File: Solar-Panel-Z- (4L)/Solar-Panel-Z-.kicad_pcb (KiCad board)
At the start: 4 copper layers, 48.4 x 48.4 mm, 88 parts, among them J1 FTS-105-01-L-DV-A, J2 U.FL-R-SMT-1, Q1 BSS138DWQ-7, Q2 MBT2222ADW1T1, Q3 BSS138DWQ-7, Q4 MBT2222ADW1T1, Q5 IRLML2803, U1 BQ25570RGRR, U2 TSL2561, U3 ATB2012-50011-T000, U4 NDS8434

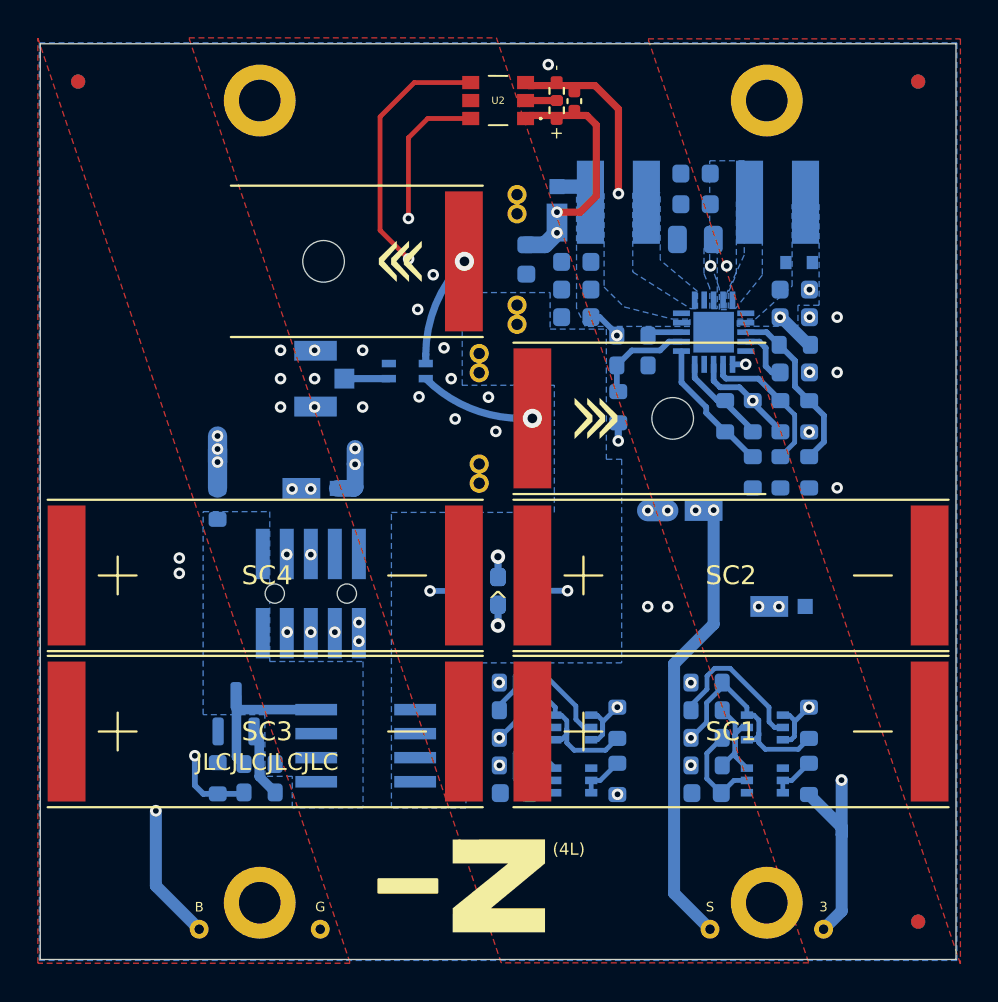
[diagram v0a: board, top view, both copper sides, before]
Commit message: Changed design to TSL2691 and IRF7404 on Z- (4L)
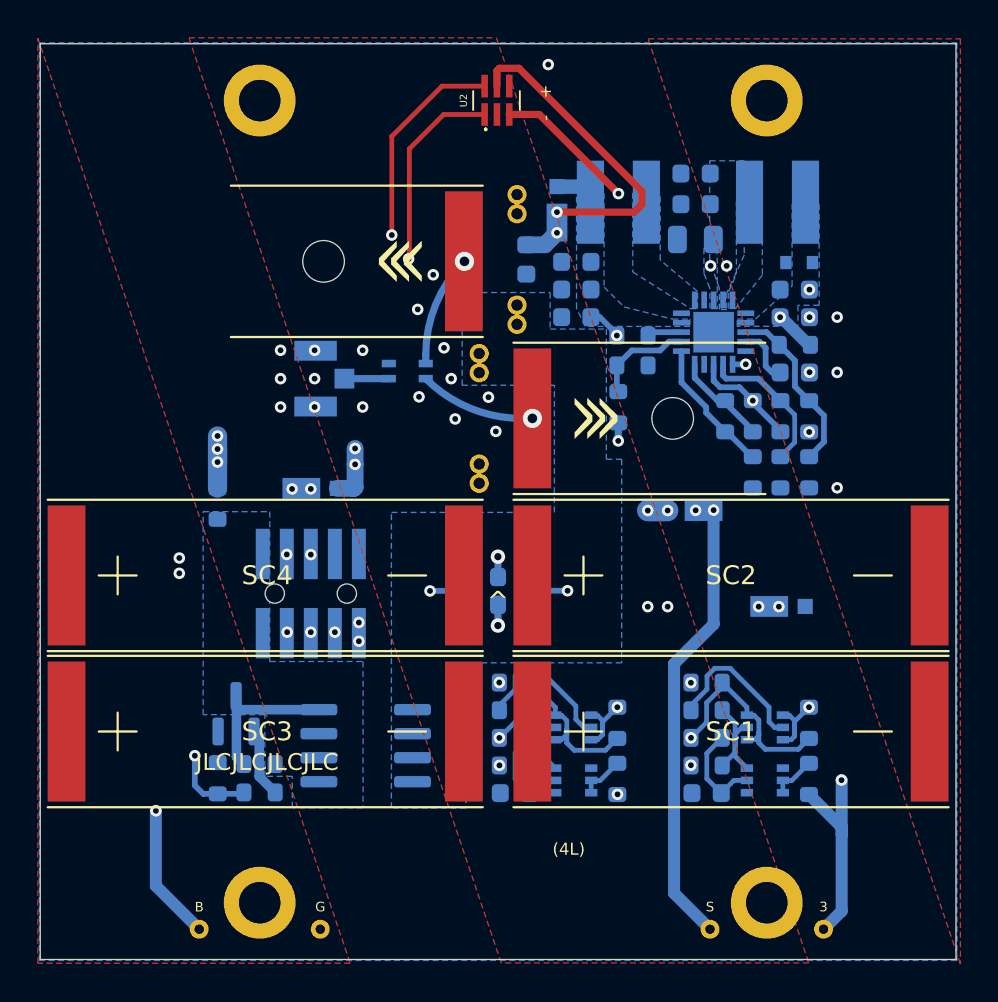
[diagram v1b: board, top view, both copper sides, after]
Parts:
- removed C1: 1uF, Capacitor_SMD:C_0402_1005Metric
- removed R1, R2: 0, Resistor_SMD:R_0402_1005Metric
- removed REF** (x6): Fiducial_0.75mm_Mask1.5mm, Fiducial:Fiducial_0.75mm_Mask1.5mm
- removed Ref**: Val**, custom-footprints:ypanel
- removed Ref**: Val**, custom-footprints:pycubed_mini_half
- U2: value TSL2561 -> TSL2591; footprint solarpanels:TSL2561 -> solarpanels:TSL2591
- U4: value NDS8434 -> IRF7404; footprint solarpanels:NDS8434 -> Package_SO:SOIC-8_3.9x4.9mm_P1.27mm
- turned U2 to 90 degrees
- turned U4 to 0 degrees
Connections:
- R5 pad 1: Net-(R5-Pad1) -> Net-(R10-Pad2)
- R6 pad 2: Net-(R5-Pad1) -> Net-(R10-Pad2)
- U1 pad 7: Net-(R5-Pad1) -> Net-(R10-Pad2)
- U2 pad 1: +3V3 -> SCL_LS
- U2 pad 2: Net-(R1-Pad1) -> unconnected-(U2-Pad2)
- U2 pad 4: SCL_LS -> unconnected-(U2-Pad4)
- U2 pad 5: unconnected-(U2-Pad5) -> +3V3
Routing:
- net Net-(R10-Pad2): track 17.1 -> 24.9 mm
- net Net-(R5-Pad1): track 7.76 -> 0.00 mm
- net +3V3: track 23.0 -> 29.6 mm
- net SCL_LS: track 62.3 -> 59.2 mm
- net GND: track 9.73 -> 7.51 mm
- net SDA_LS: track 49.8 -> 51.8 mm
- net Net-(R1-Pad1): track 1.64 -> 0.00 mm

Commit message: Changed TSL2591 to BH1750
All boards (4L) except -Y
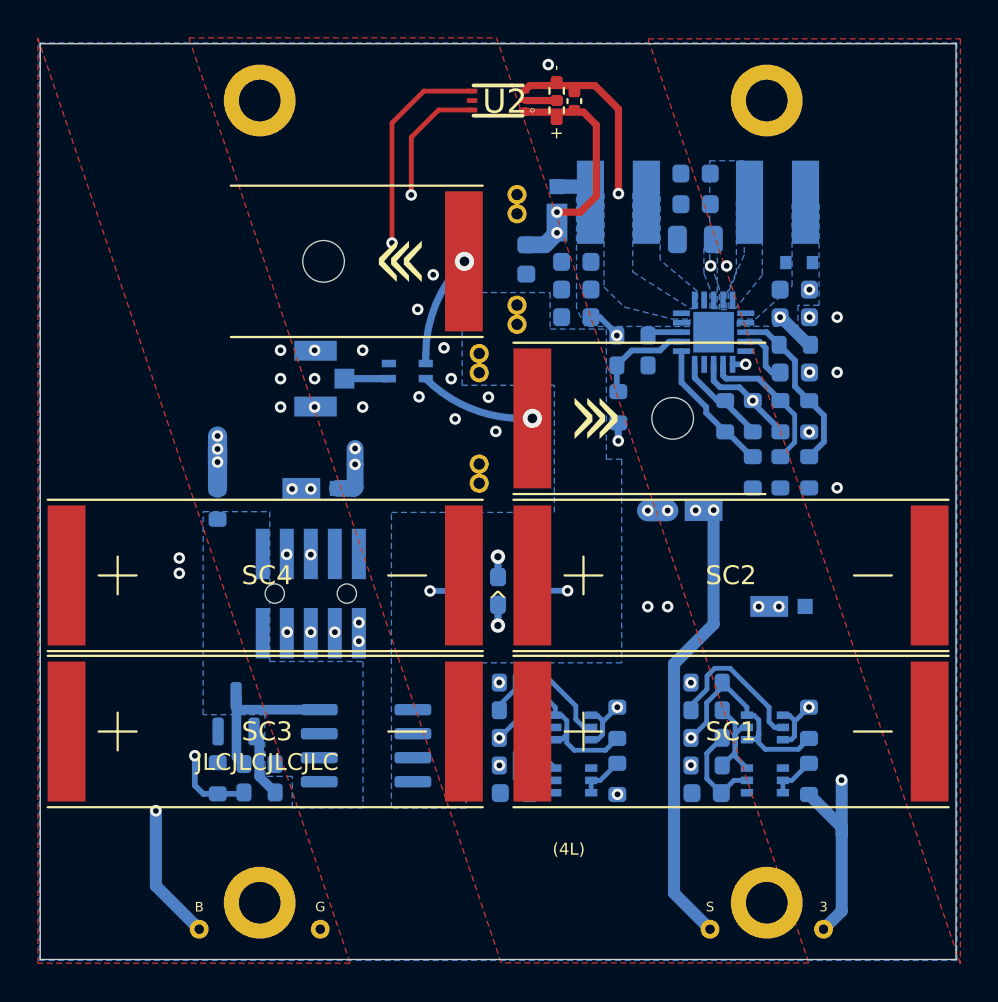
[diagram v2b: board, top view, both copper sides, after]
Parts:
- added C1: 1uF, Capacitor_SMD:C_0402_1005Metric, F.Cu at (110.7, 45.3)
- added R1: 0, Resistor_SMD:R_0402_1005Metric, F.Cu at (109.8, 45.8)
- added R2: 0, Resistor_SMD:R_0402_1005Metric, F.Cu at (109.8, 44.8)
- U2: value TSL2591 -> BH1750FVI-TR; footprint solarpanels:TSL2591 -> solarpanels:WSOF6
- turned U2 to 180 degrees
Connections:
- U2 pad 1: SCL_LS -> +3V3
- U2 pad 2: unconnected-(U2-Pad2) -> Net-(R1-Pad1)
- U2 pad 4: unconnected-(U2-Pad4) -> SDA_LS
- U2 pad 5: +3V3 -> unconnected-(U2-Pad5)
- U2 pad 6: SDA_LS -> SCL_LS
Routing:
- net +3V3: track 29.6 -> 23.3 mm
- net GND: track 7.51 -> 10.0 mm
- net Net-(R1-Pad1): track 0.00 -> 1.64 mm

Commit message: Updated light sensor to OPT 3001, Updated solar diodes.
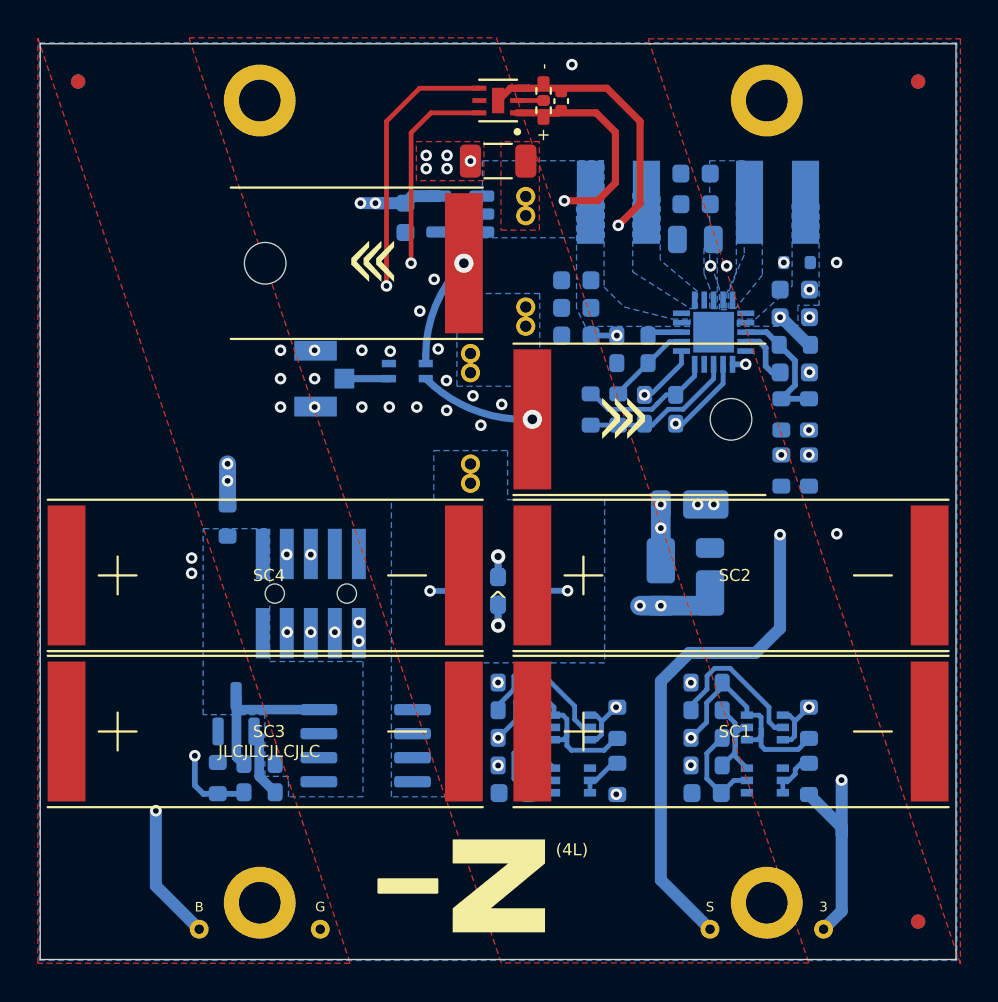
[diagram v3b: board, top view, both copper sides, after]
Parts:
- removed D5: MSS1P4-M3_89A, solarpanels:MICROSMP
- removed R31: 10K, Resistor_SMD:R_0603_1608Metric
- added Q6: IRF7404, Package_SO:SOIC-8_3.9x4.9mm_P1.27mm, B.Cu at (99.7, 79.4)
- added R34: 100K, Resistor_SMD:R_0603_1608Metric, B.Cu at (94.1, 80.4)
- added R35: 1R, Resistor_SMD:R_1206_3216Metric, F.Cu at (106.7, 48.5)
- added REF**: Fiducial_0.75mm_Mask1.5mm, Fiducial:Fiducial_0.75mm_Mask1.5mm, F.Cu at (128.9, 88.7)
- added REF**: Fiducial_0.75mm_Mask1.5mm, Fiducial:Fiducial_0.75mm_Mask1.5mm, F.Cu at (128.9, 44.3)
- added REF**: Fiducial_0.75mm_Mask1.5mm, Fiducial:Fiducial_0.75mm_Mask1.5mm, F.Cu at (84.5, 44.3)
- added REF**: Fiducial_0.75mm_Mask1.5mm, Fiducial:Fiducial_0.75mm_Mask1.5mm, B.Cu at (128.9, 44.3)
- added REF**: Fiducial_0.75mm_Mask1.5mm, Fiducial:Fiducial_0.75mm_Mask1.5mm, B.Cu at (128.9, 88.7)
- added REF**: Fiducial_0.75mm_Mask1.5mm, Fiducial:Fiducial_0.75mm_Mask1.5mm, B.Cu at (84.5, 44.3)
- added Ref**: Val**, custom-footprints:ypanel, F.Cu at (106.1, 86.6)
- added Ref**: Val**, custom-footprints:pycubed_mini_half, B.Cu at (106.8, 44.6)
- D2, D3, D4: value MSS1P4-M3_89A -> DFLS130L-7; footprint solarpanels:MICROSMP -> Diode_SMD:D_PowerDI-123
- J1: value FTS-105-01-L-DV-A -> FTS-105-01-X-DV-A
- J2: footprint solarpanels:U.FL-R-SMT-1 -> mainboard:U.FL-R-SMT-1
- JP1: value Jumper -> BurnWire 1
- JP2: value Jumper -> BurnWire 2
- Q1, Q3: value BSS138DWQ-7 -> NX3008NBKS
- R1, R12, R13, R16, R17, R18, R2, R3, R4: value 0 -> 0R
- R14, R15, R19, R20: value DNI -> DNI (0R)
- R21, R26: value 680 -> 680R
- R32: value 4.7K -> 10K
- R33: value 100K -> 4.7K
- U2: value BH1750FVI-TR -> OPT3001; footprint solarpanels:WSOF6 -> solarpanels:OPT3001
- U4: value IRF7404 -> MAX40200AUK; footprint Package_SO:SOIC-8_3.9x4.9mm_P1.27mm -> Package_TO_SOT_SMD:SOT-23-5
- moved U4 28.5 mm to (104.7, 51.3), turned to 180 degrees
- moved D4 18.9 mm to (115.3, 70.5), turned to -90 degrees
- moved D2 17.1 mm to (116.8, 66.7), turned to 180 degrees
- moved JP1 8.75 mm to (105.2, 62.1)
- moved JP2 8.66 mm to (108.2, 53.8), turned to 0 degrees
- moved R7 8.58 mm to (111.6, 61.6), turned to -90 degrees
- moved C11 6.76 mm to (101.8, 51.5)
- moved R5 6.37 mm to (115.3, 62.4), turned to 180 degrees
- moved D3 4.09 mm to (117.9, 70.5), turned to 90 degrees
- moved R8 3.62 mm to (115.3, 60.9), turned to 0 degrees
- moved R15 3.39 mm to (121.7, 61.9)
- moved R32 2.34 mm to (91.9, 81.1), turned to 90 degrees
- moved R9 1.51 mm to (121.7, 64.9)
- moved R6 1.51 mm to (123.1, 64.9)
- moved R33 1.49 mm to (94.1, 81.9), turned to 180 degrees
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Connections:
- C10 pad 1: Net-(C10-Pad1) -> Net-(U1-VOUT)
- C8 pad 1: Net-(C10-Pad1) -> Net-(U1-VOUT)
- D2 pad 1: +3V3 -> VSOLAR
- D2 pad 2: Net-(C10-Pad1) -> /VSOLAR_FULL
- JP1 pad 2: GND -> Net-(JP1-Pad2)
- JP2 pad 1: /VBURN -> Net-(JP1-Pad2)
- JP2 pad 2: GND -> Net-(JP2-Pad2)
- L2 pad 2: Net-(C10-Pad1) -> Net-(U1-VOUT)
- Q5 pad 1: Net-(Q5-Pad1) -> Net-(Q5-G)
- Q5 pad 3: Net-(Q5-Pad3) -> Net-(Q5-D)
- R10 pad 2: Net-(R10-Pad2) -> Net-(U1-VRDIV)
- R32 pad 1: Net-(Q5-Pad1) -> BURN1
- R32 pad 2: BURN1 -> GND
- R33 pad 1: Net-(Q5-Pad3) -> Net-(Q5-G)
- R33 pad 2: BATT_P -> BURN1
- R5 pad 1: Net-(R10-Pad2) -> Net-(U1-VBAT_OV)
- R5 pad 2: Net-(R10-Pad2) -> Net-(U1-VRDIV)
- R6 pad 2: Net-(R10-Pad2) -> Net-(U1-VBAT_OV)
- R7 pad 2: Net-(R10-Pad2) -> Net-(U1-VRDIV)
- U1 pad 14: Net-(C10-Pad1) -> Net-(U1-VOUT)
- U1 pad 7: Net-(R10-Pad2) -> Net-(U1-VBAT_OV)
- U1 pad 8: Net-(R10-Pad2) -> Net-(U1-VRDIV)
- U2 pad 4: SDA_LS -> SCL_LS
- U2 pad 6: SCL_LS -> SDA_LS
- U4 pad 1: BATT_P -> Net-(U1-VOUT)
- U4 pad 2: BATT_P -> GND
- U4 pad 3: BATT_P -> Net-(U1-VOUT)
- U4 pad 4: Net-(Q5-Pad3) -> unconnected-(U4-NC-Pad4)
- U4 pad 5: /VBURN -> +3V3
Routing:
- net Net-(R10-Pad2): track 24.9 -> 0.00 mm, vias 2 -> 0
- net Net-(U1-VBAT_OV): track 0.00 -> 15.7 mm, vias 0 -> 2
- net VSOLAR: track 43.6 -> 56.7 mm, vias 4 -> 5
- net Net-(Q5-Pad3): track 8.70 -> 0.00 mm
- net Net-(Q5-D): track 0.00 -> 8.70 mm
- net Net-(U1-VRDIV): track 0.00 -> 8.28 mm
- net SCL_LS: track 59.0 -> 65.5 mm
- net Net-(U1-OK_PROG): track 7.08 -> 13.0 mm, vias 0 -> 2
- net Net-(D3-K): track 9.94 -> 4.38 mm, vias 6 -> 2
- net GND: track 10.0 -> 15.1 mm, vias 22 -> 30
- net +3V3: track 23.3 -> 28.3 mm, vias 10 -> 11
- net SDA_LS: track 51.4 -> 55.2 mm
- net Net-(Q5-Pad1): track 3.68 -> 0.00 mm
- net Net-(Q5-G): track 0.00 -> 3.68 mm
- net Net-(U1-OK_HYST): track 4.89 -> 7.23 mm
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- added copper zone on In1.Cu, net GND
- added copper zone on B.Cu, net Net-(JP1-Pad2)
- added copper zone on In1.Cu, net Net-(JP1-Pad2)
- added copper zone on F.Cu, net Net-(JP2-Pad2)
- added copper zone on B.Cu, net Net-(U1-VOUT)
- removed copper zone on B.Cu, net Net-(C10-Pad1)
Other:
- board text added: "Rev B3/01"
- board text removed: "Rev B2/01"

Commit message: Silkscreen fix for -Z antenna wire
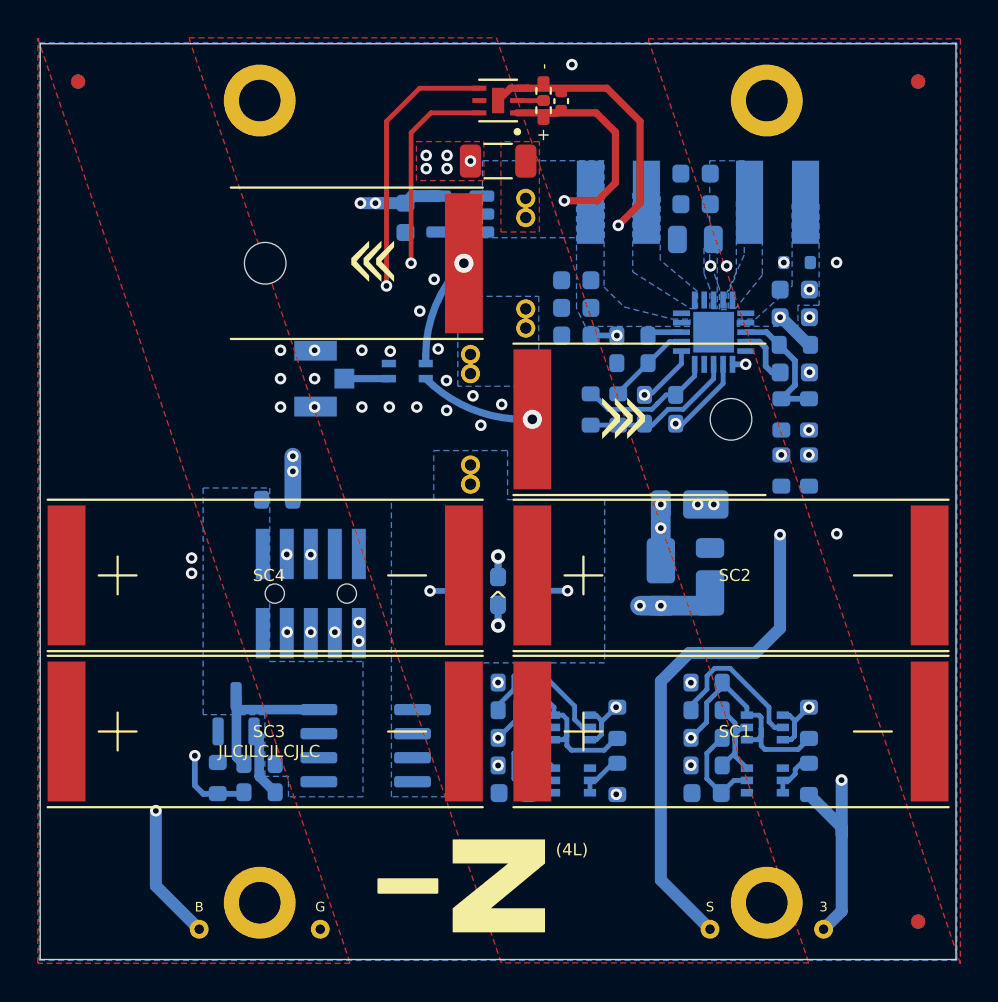
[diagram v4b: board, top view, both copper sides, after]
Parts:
- moved R3 2.85 mm to (95.0, 66.4), turned to 0 degrees
- moved JP2 0.10 mm to (108.2, 53.9)
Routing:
- net VBAT: track 9.01 -> 9.51 mm
